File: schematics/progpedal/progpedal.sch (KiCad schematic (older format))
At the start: 11 parts, among them U1 TL072

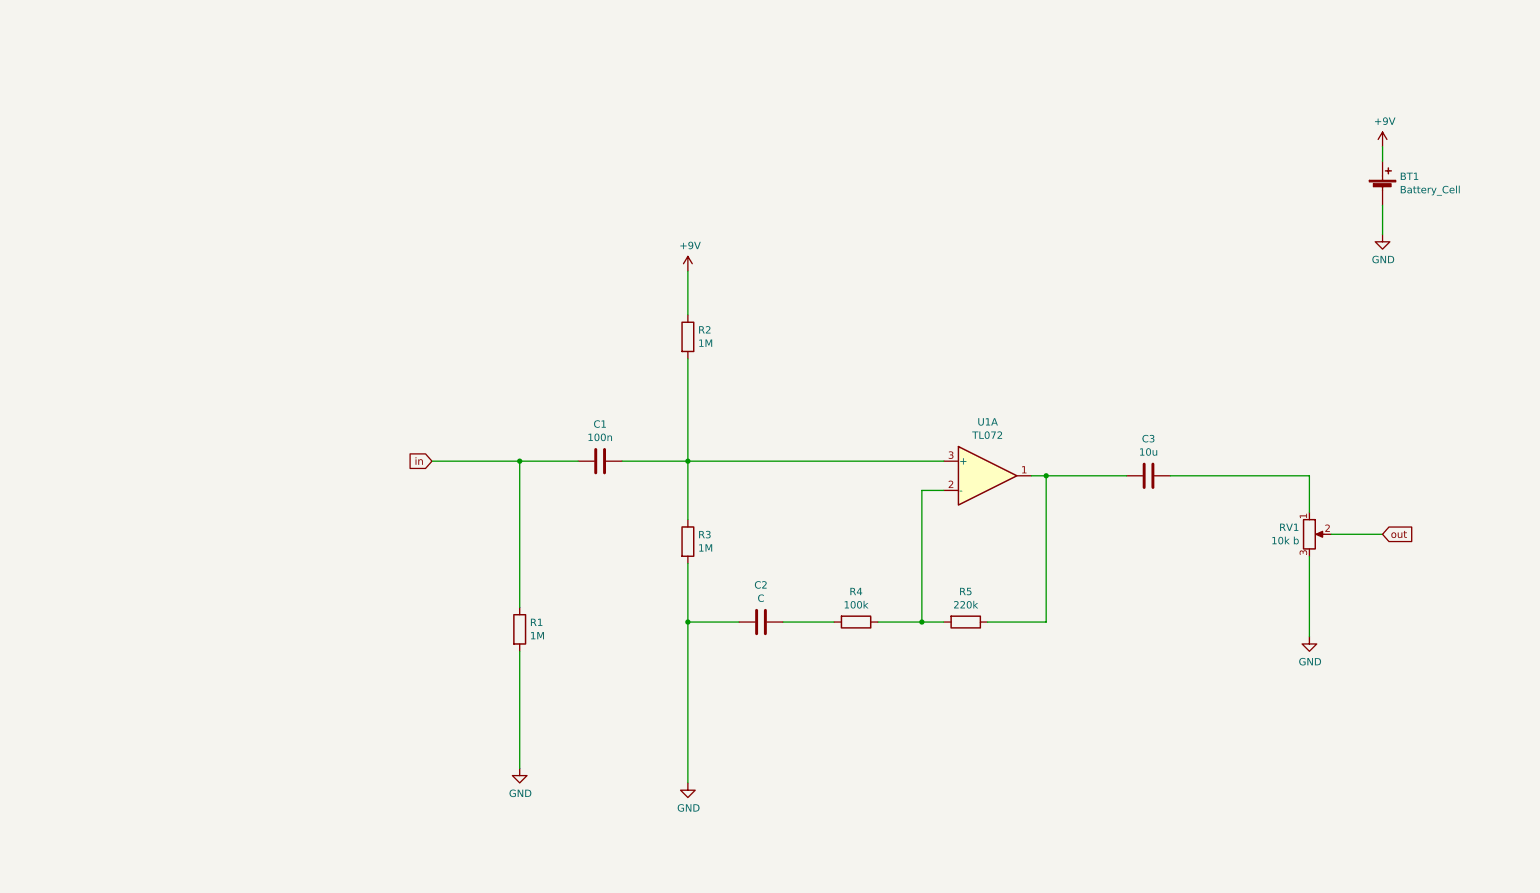
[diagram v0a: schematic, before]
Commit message: add draft of output section schematic
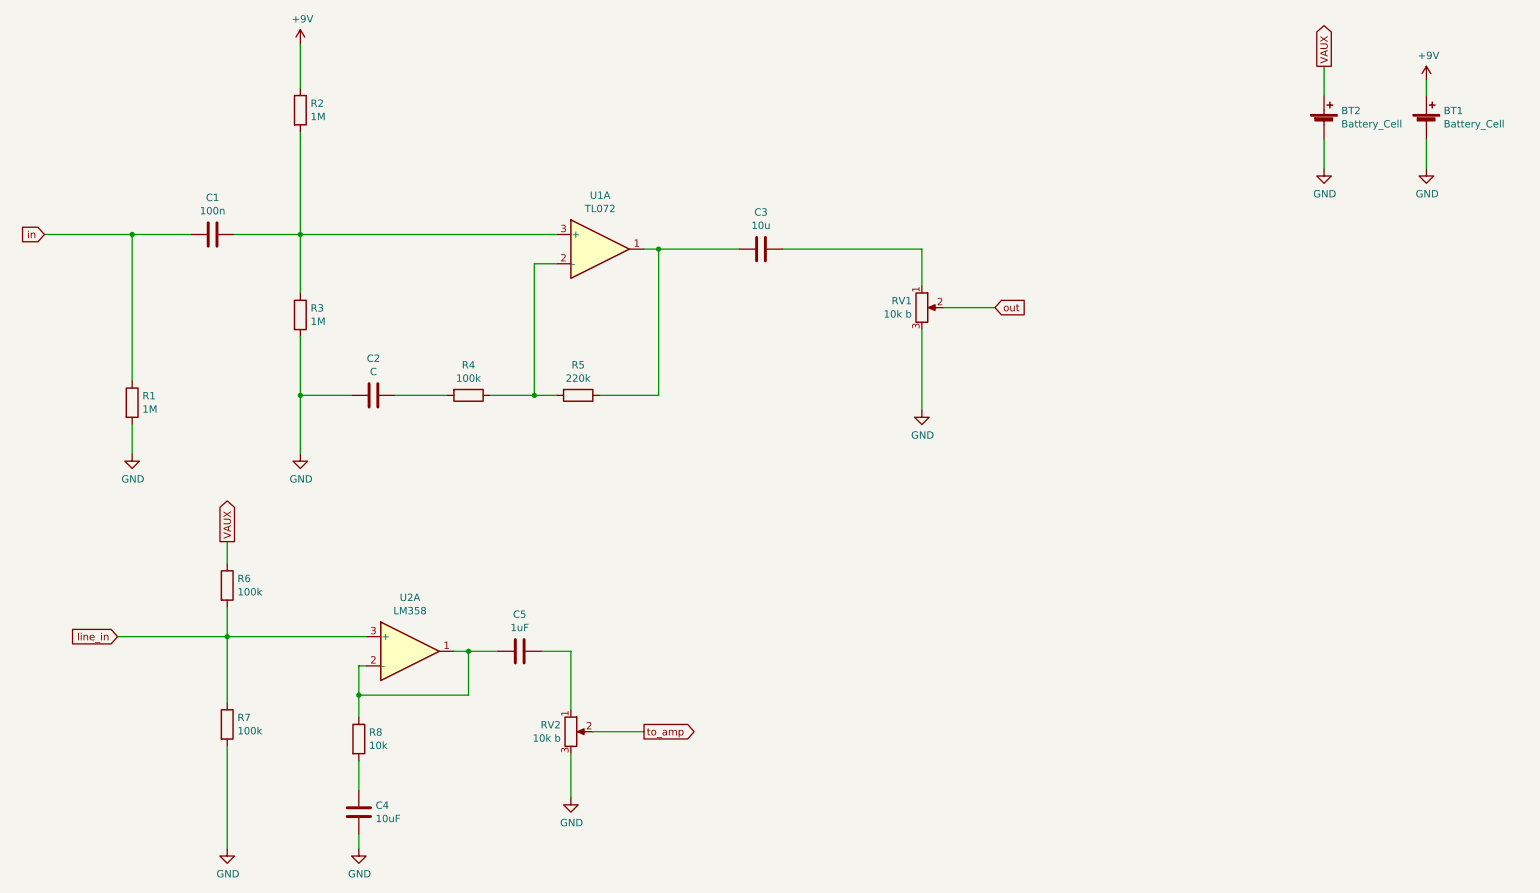
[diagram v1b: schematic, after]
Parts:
- added BT2: Battery_Cell, symbol Device:Battery_Cell
- added C4: 10uF, symbol Device:C
- added C5: 1uF, symbol Device:C
- added R6, R7: 100k, symbol Device:R
- added R8: 10k, symbol Device:R
- added RV2: 10k b, symbol Device:R_POT
- added U2: LM358, symbol Amplifier_Operational:LM358
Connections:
- net GND: now also BT2.2 (-), C4.2, R7.2, RV2.3
- new net: C5.2, R8.1, U2.1, U2.2 (-)
- new net: C4.1, R8.2
- new net: C5.1, RV2.1
- new net VAUX: BT2.1 (+), R6.1
- new net line_in: R6.2, R7.1, U2.3 (+)
- new net to_amp: RV2.2
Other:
- moved on the sheet: BT1, C1, C2, C3, R1, R2, R3, R4, R5, RV1, U1A

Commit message: Add voltage regulator to schematic
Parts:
- added C6, C7: 10u, symbol Device:C
- added U3: L7805, symbol Regulator_Linear:L7805
- C5: value 1uF -> 10uF
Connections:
- net +9V: now also C6.2, U3.1 (IN)
- net GND: now also C6.1, C7.1, U3.2 (GND)
- net VAUX: now also C7.2, U3.3 (OUT)
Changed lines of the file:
@@
 P 4050 5000
 F 0 "C5" V 3798 5000 50  0000 C CNN
-F 1 "1uF" V 3889 5000 50  0000 C CNN
+F 1 "10uF" V 3889 5000 50  0000 C CNN
 F 2 "" H 4088 4850 50  0001 C CNN
 F 3 "~" H 4050 5000 50  0001 C CNN
@@
 Wire Wire Line
 	2050 4400 2050 4250
+$Comp
+L Regulator_Linear:L7805 U3
+U 1 1 60EAE80D
+P 8750 4450
+F 0 "U3" H 8750 4692 50  0000 C CNN
+F 1 "L7805" H 8750 4601 50  0000 C CNN
+F 2 "" H 8775 4300 50  0001 L CIN
+F 3 "http://www.st.com/content/ccc/resource/technical/document/datasheet/41/4f/b3/b0/12/d4/47/88/CD00000444.pdf/files/CD00000444.pdf/jcr:content/translations/en.CD00000444.pdf" H 8750 4400 50  0001 C CNN
+	1    8750 4450
+	1    0    0    -1
+$EndComp
+$Comp
+L Device:C C6
+U 1 1 60EAEE6A
+P 7950 5100
+F 0 "C6" H 7650 5100 50  0000 C CNN
+F 1 "10u" H 7789 5100 50  0000 C CNN
+F 2 "" H 7988 4950 50  0001 C CNN
+F 3 "~" H 7950 5100 50  0001 C CNN
+	1    7950 5100
+	-1   0    0    1
+$EndComp
+$Comp
+L Device:C C7
+U 1 1 60EB03F6
+P 9400 5100
+F 0 "C7" H 9100 5100 50  0000 C CNN
+F 1 "10u" H 9239 5100 50  0000 C CNN
+F 2 "" H 9438 4950 50  0001 C CNN
+F 3 "~" H 9400 5100 50  0001 C CNN
+	1    9400 5100
+	-1   0    0    1
+$EndComp
+$Comp
+L power:GND #PWR012
+U 1 1 60EB2BDF
+P 7950 5500
+F 0 "#PWR012" H 7950 5250 50  0001 C CNN
+F 1 "GND" H 7955 5327 50  0000 C CNN
+F 2 "" H 7950 5500 50  0001 C CNN
+F 3 "" H 7950 5500 50  0001 C CNN
+	1    7950 5500
+	1    0    0    -1
+$EndComp
+$Comp
+L power:GND #PWR013
+U 1 1 60EB32EC
+P 8750 5500
+F 0 "#PWR013" H 8750 5250 50  0001 C CNN
+F 1 "GND" H 8755 5327 50  0000 C CNN
+F 2 "" H 8750 5500 50  0001 C CNN
+F 3 "" H 8750 5500 50  0001 C CNN
+	1    8750 5500
+	1    0    0    -1
+$EndComp
+$Comp
+L power:GND #PWR014
+U 1 1 60EB3A0C
+P 9400 5500
+F 0 "#PWR014" H 9400 5250 50  0001 C CNN
+F 1 "GND" H 9405 5327 50  0000 C CNN
+F 2 "" H 9400 5500 50  0001 C CNN
+F 3 "" H 9400 5500 50  0001 C CNN
+	1    9400 5500
+	1    0    0    -1
+$EndComp
+$Comp
+L power:+9V #PWR011
+U 1 1 60EB42A7
+P 7950 4200
+F 0 "#PWR011" H 7950 4050 50  0001 C CNN
+F 1 "+9V" H 7965 4373 50  0000 C CNN
+F 2 "" H 7950 4200 50  0001 C CNN
+F 3 "" H 7950 4200 50  0001 C CNN
+	1    7950 4200
+	1    0    0    -1
+$EndComp
+Text GLabel 9400 4200 1    50   Output ~ 0
+VAUX
+Wire Wire Line
+	7950 4950 7950 4450
+Wire Wire Line
+	7950 5500 7950 5250
+Wire Wire Line
+	8750 5500 8750 4750
+Wire Wire Line
+	9400 5500 9400 5250
+Wire Wire Line
+	9400 4950 9400 4450
+Wire Wire Line
+	9050 4450 9400 4450
+Connection ~ 9400 4450
+Wire Wire Line
+	9400 4450 9400 4200
+Wire Wire Line
+	8450 4450 7950 4450
+Connection ~ 7950 4450
+Wire Wire Line
+	7950 4450 7950 4200
 $EndSCHEMATC
